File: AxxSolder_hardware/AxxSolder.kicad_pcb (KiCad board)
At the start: 2 copper layers, 39 x 82.5 mm, 147 parts, among them IC1 TLV76733DRVR, IC2 OPA2387DSGT, IC3 LMR54406DBVR, IC4 STM32G431CBT6, IC5 TPD4E1U06DBVR, IC6 STUSB4500QTR, IC7 MAX16171ATA_VY+T, IC8 LTC4440AHMS8E, IC9 INA281A5QDBVRQ1, J1 USB4110-GF-A, J2 691243110009, J3 TSW-102-07-T-S, J4 61300611821, J5 TSW-102-07-T-S, J6 TSW-102-07-T-S, J7 TSW-108-07-T-S, Q1 STL9P3LLH6, Q2 STL10N3LLH5, Q3 2N7002NXAKR, U2 PEC11J-9215F-S0015, U3 BSC014N04LS

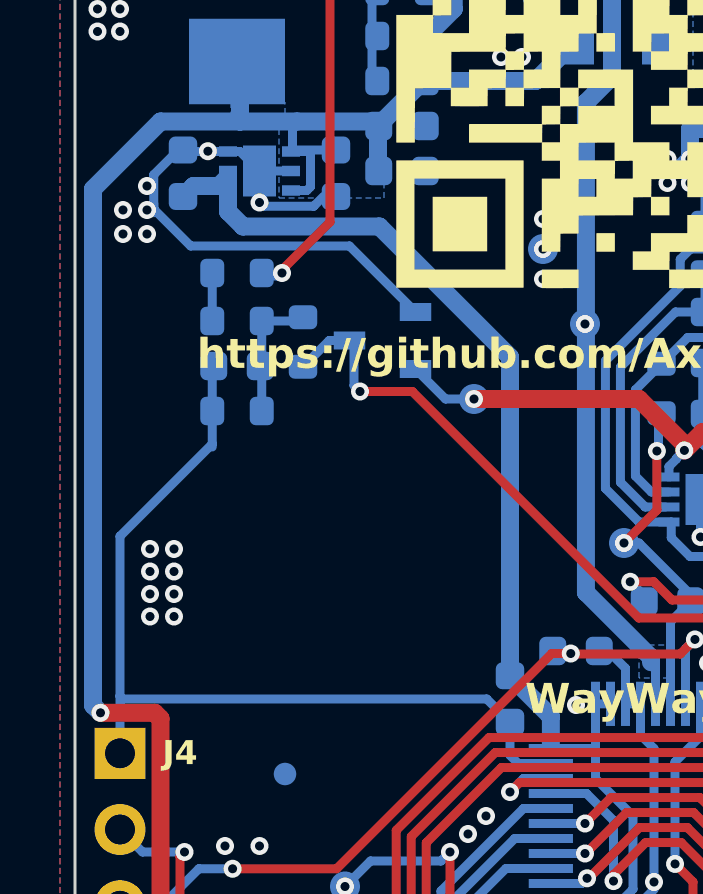
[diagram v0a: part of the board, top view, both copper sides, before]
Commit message: added pwr connections for relay add on board
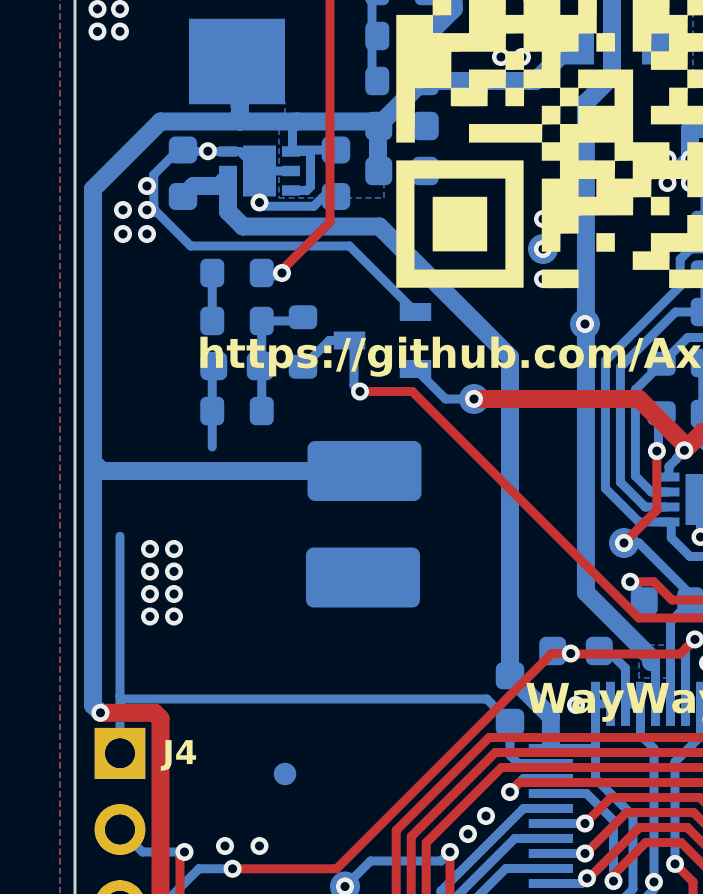
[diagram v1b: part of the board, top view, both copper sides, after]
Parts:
- added 7.5V: RELAY, TestPoint:TestPoint_Keystone_5019_Miniature, B.Cu at (170.7, 99.9)
- added G: GND, TestPoint:TestPoint_Keystone_5019_Miniature, B.Cu at (170.6, 103.5)
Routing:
- net +7.5V: track 94.3 -> 103.5 mm
- net GND: track 435.4 -> 431.1 mm
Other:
- board text added: "Oct 25"
- board text added: "Rev1 DC"
- board text removed: "2025-03"
- board text removed: "AxxAxx"

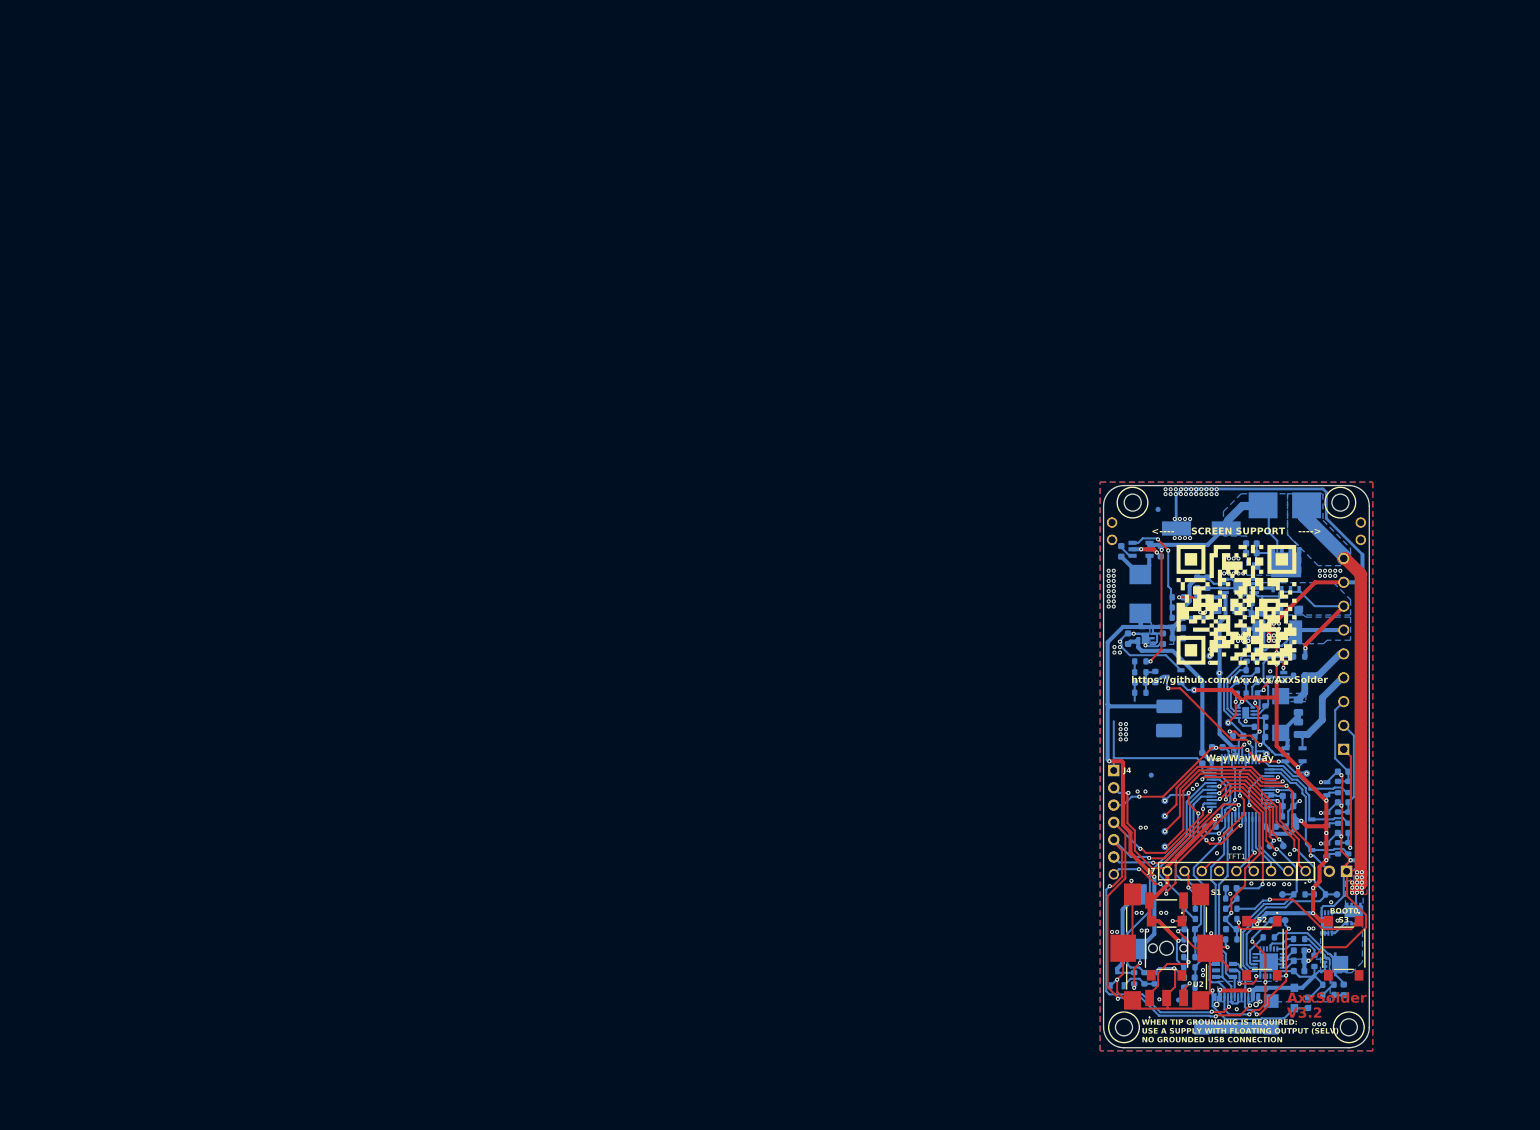
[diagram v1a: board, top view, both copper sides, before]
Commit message: enlarged PCB
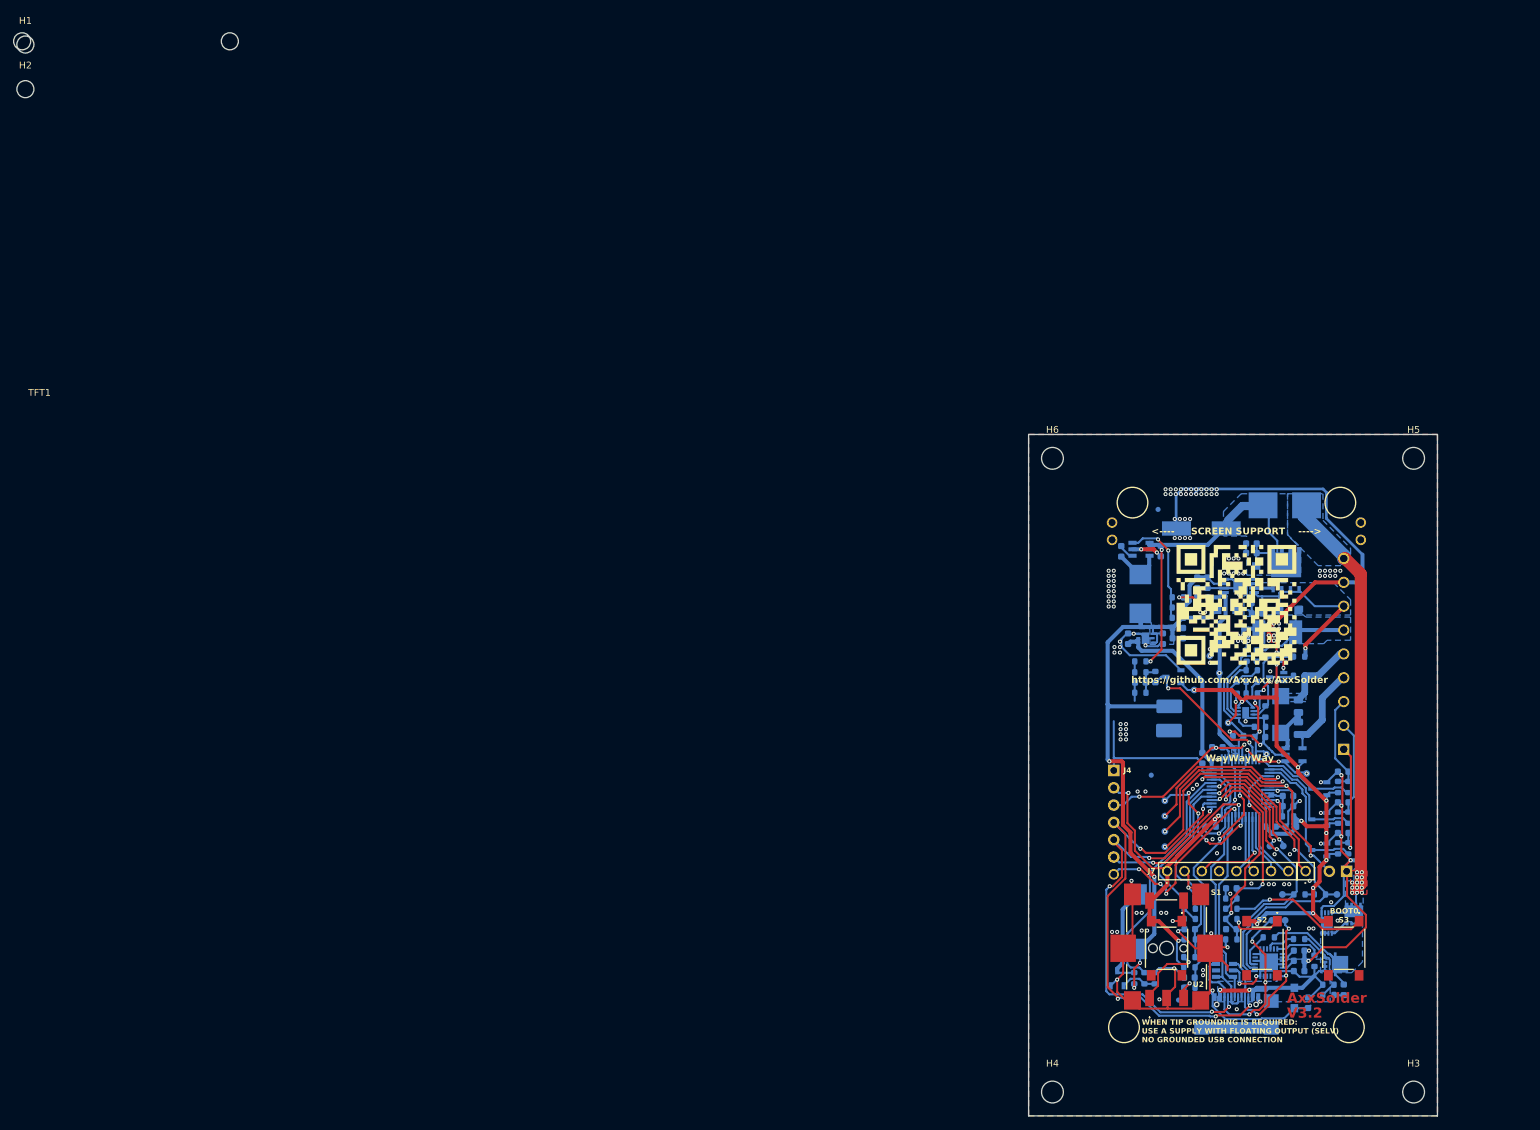
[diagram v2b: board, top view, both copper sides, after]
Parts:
- added H3: MountingHole, MountingHole:MountingHole_3.2mm_M3, F.Cu at (206.5, 156.5)
- added H4: MountingHole, MountingHole:MountingHole_3.2mm_M3, F.Cu at (153.5, 156.5)
- added H5: MountingHole, MountingHole:MountingHole_3.2mm_M3, F.Cu at (206.5, 63.5)
- added H6: MountingHole, MountingHole:MountingHole_3.2mm_M3, F.Cu at (153.5, 63.5)
- moved H2 238.1 mm to (2.77, 9.32)
- moved H1 216.3 mm to (2.77, 2.77)
- moved TFT1 176.5 mm to (17.5, 58.9)
- renumbered 7.5V to 7.5, G to Gnd1
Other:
- board size 39 x 82.5 mm -> 60 x 100 mm

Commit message: enlarged board
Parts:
- removed H1, H2: MountingHole, MountingHole:MountingHole_2.5mm
- removed S1: ADTSM644RVTR, footprints:ADTSM644RVTR
- removed TP18: DIAG_TP, footprints:TSW-101-XX-YY-S
- added J8: Conn_01x01_Pin, footprints:TSW-101-XX-YY-S, F.Cu at (190.6, 124.1)
- added J9: TSW-102-07-T-S, footprints:TSW-102-XX-YY-S, F.Cu at (157.4, 99.6)
- moved TFT1 110.4 mm to (103.7, 128.0)
- moved H3 12.5 mm to (219.0, 156.0)
- moved H5 12.5 mm to (219.0, 64.0)
- moved H4 11.5 mm to (142.0, 156.0)
- moved H6 11.5 mm to (142.0, 64.0)
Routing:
- net +7.5V: track 103.5 -> 107.7 mm
- net /SD_CS: track 13.3 -> 15.2 mm
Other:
- board size 60 x 100 mm -> 85 x 100 mm

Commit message: Update AxxSolder.kicad_pcb
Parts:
- added G***: LOGO, SubmarineCircuits:SubmarineCircuits_30x20mm text, F.Cu at (208.6, 121.9)
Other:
- board text added: "Remixed from https://github.com/AxxAxx/AxxSolder SubmarineCircuits@gmail.com Rev 1 17/10/25"

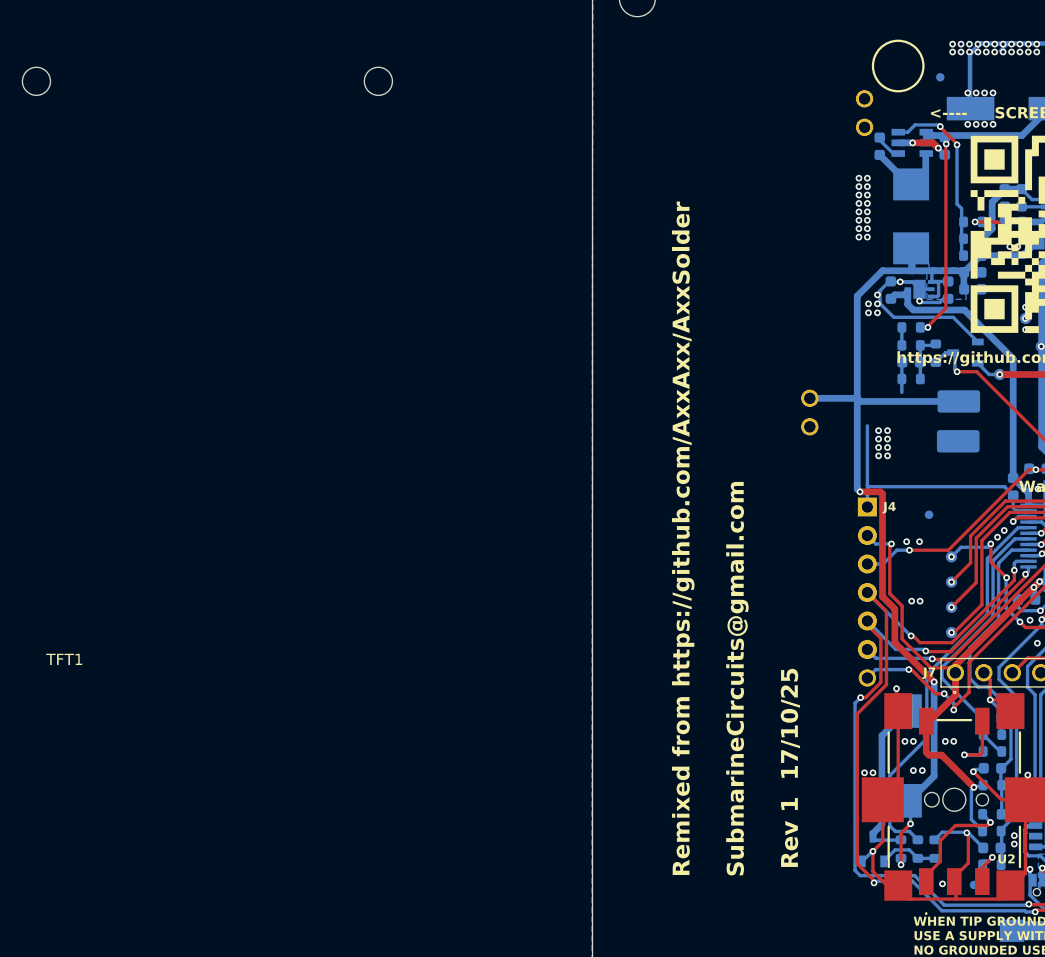
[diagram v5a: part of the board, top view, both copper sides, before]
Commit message: deleted fuducials
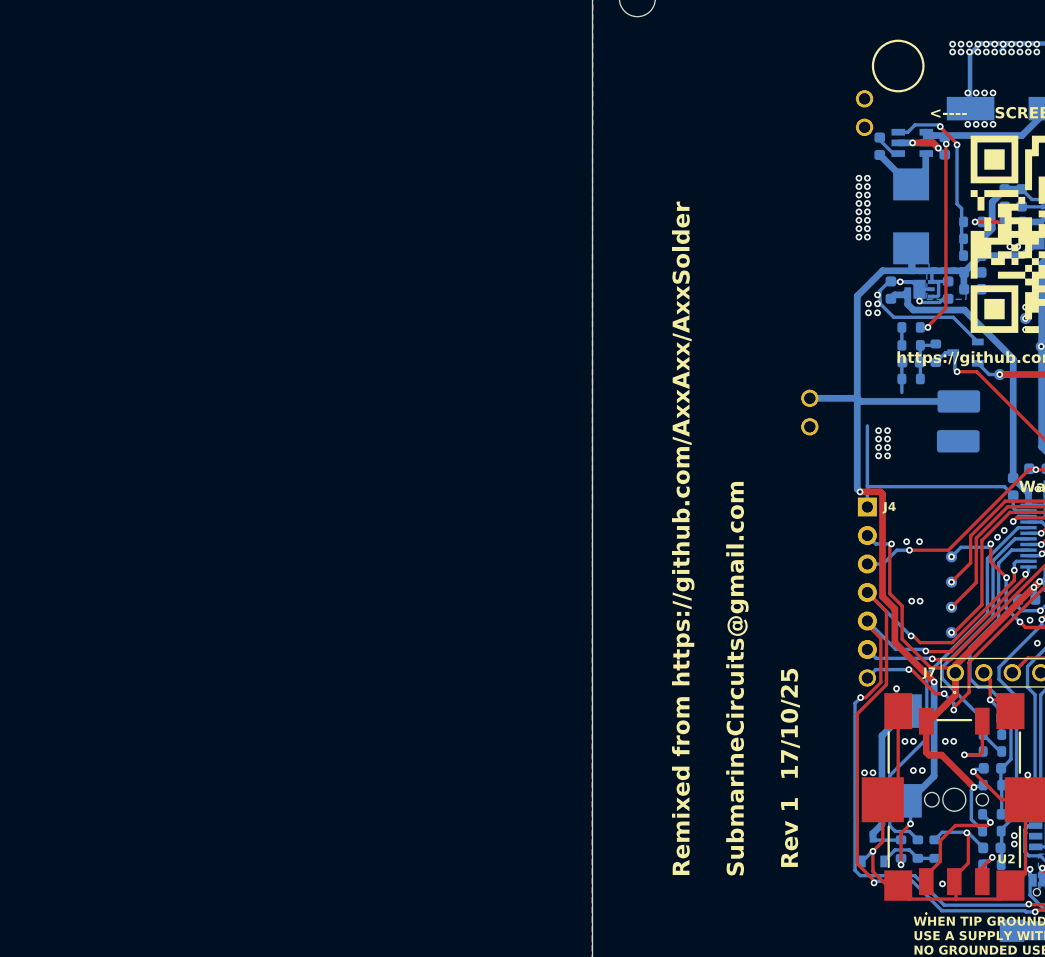
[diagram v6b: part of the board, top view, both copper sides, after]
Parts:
- removed FID1, FID2, FID3: Fiducial, Fiducial:Fiducial_0.75mm_Mask1.5mm
- removed TFT1: ~, footprints:Adafruit_240x320_TFT

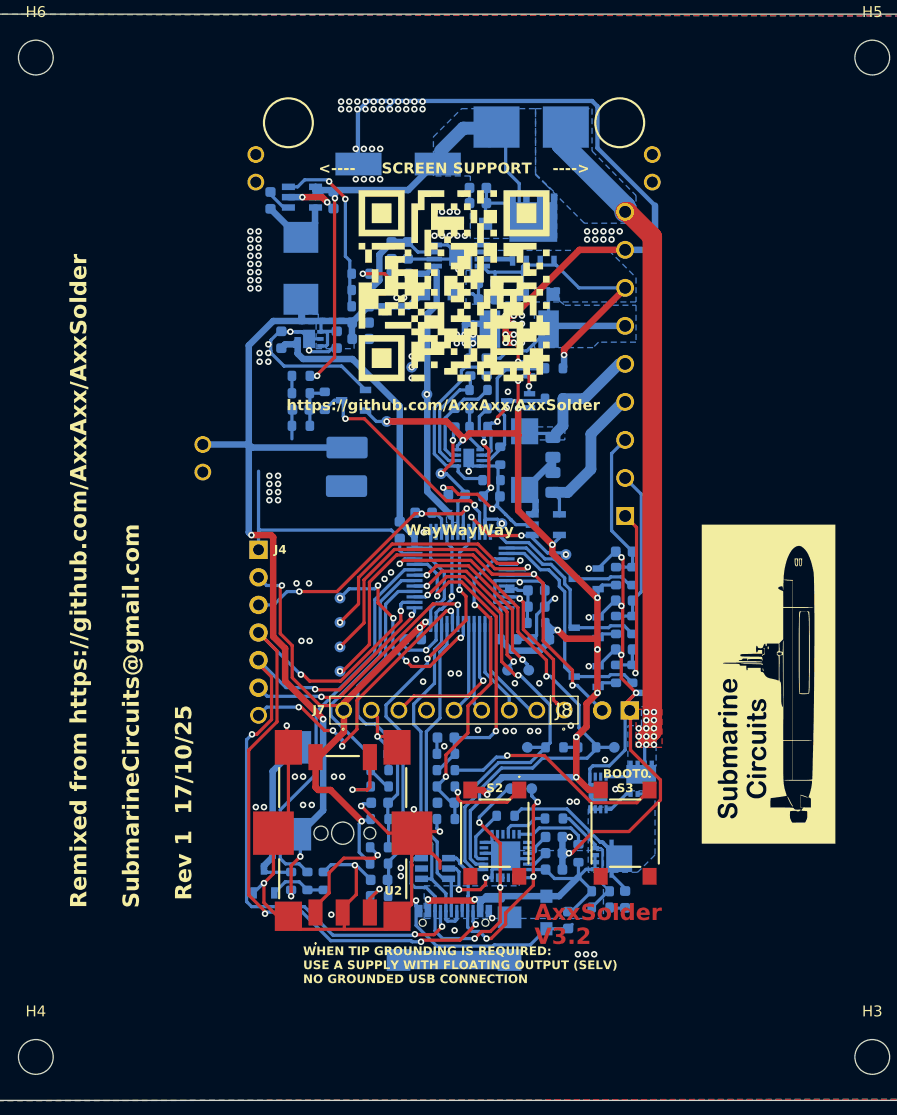
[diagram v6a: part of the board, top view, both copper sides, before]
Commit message: added stitching vias
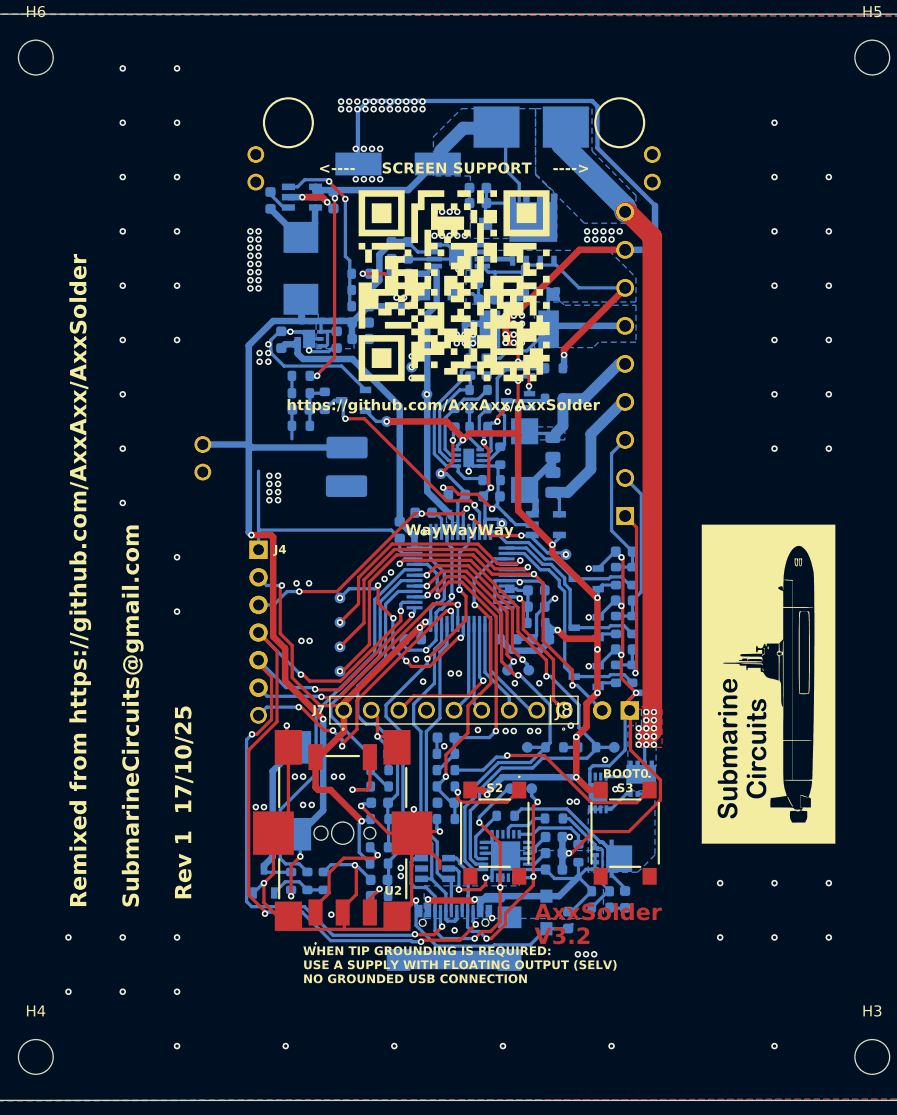
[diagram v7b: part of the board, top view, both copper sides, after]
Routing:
- net GND: vias 176 -> 224
